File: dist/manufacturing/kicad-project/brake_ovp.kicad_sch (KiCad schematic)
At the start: 13 parts, among them J3 B2P-VH(LF)(SN), Q16 CSD19534Q5A, U14 TLV3201AIDBVR, U15 UCC27511DBVR

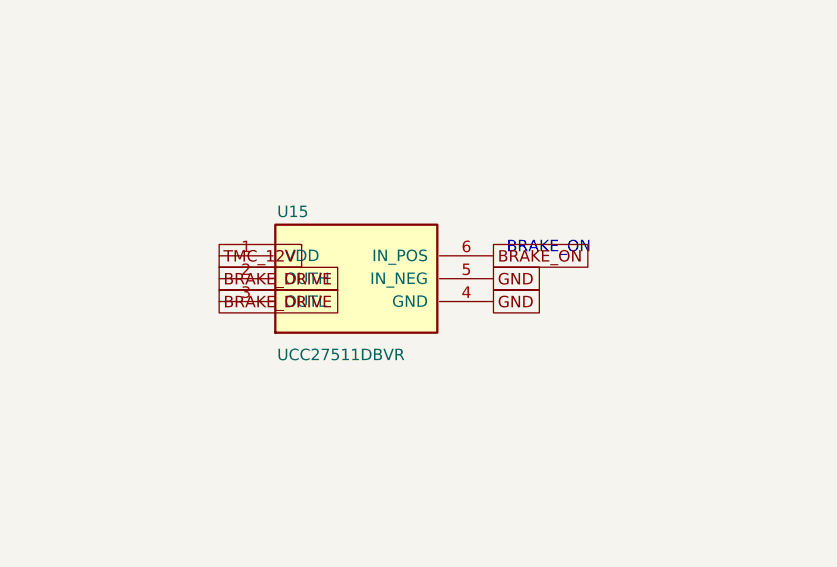
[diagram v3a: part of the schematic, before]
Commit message: Replace unavailable MCU and expander with stocked JLC parts
Use STM32G0B1CEU6 with a grounded UFQFPN48 exposed pad and a 512 KiB
firmware/readback target. Use PCA9538PWR with a PD-powered reset buffer,
bypass capacitor and pulldown to address independent-rail reset injection.

Regenerate local routing, native/manufacturing artifacts, assembly data,
stock evidence and the routed viewer. Preserve unrelated copper and holes
with the existing protected projection. Retain motion locks and physical
qualification holds. Preserve quoted DSN net names and native EP paste sizing.
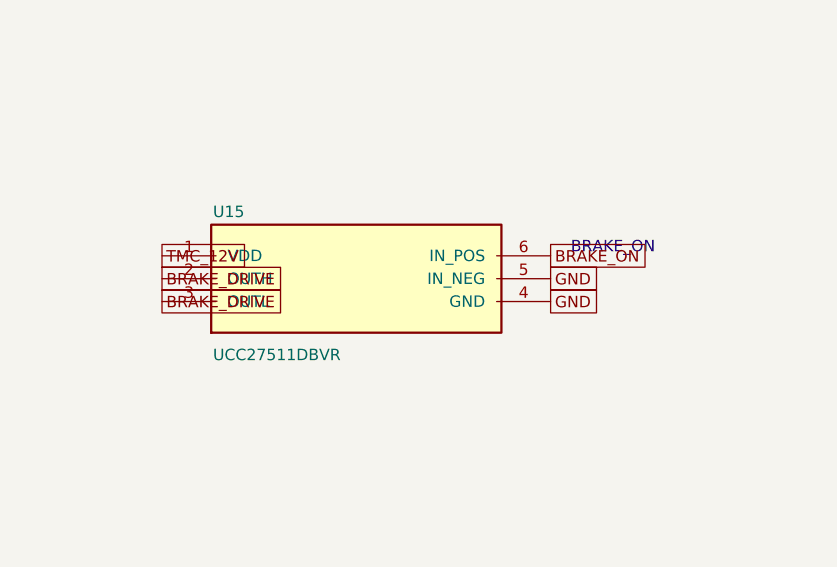
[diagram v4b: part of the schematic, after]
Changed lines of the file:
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@@
     (instances
       (project ""
-        (path "/857a17cf-af0e-42f8-87e7-32303329b4d2/9c455ead-0a67-4132-9c5a-187d55c8c2bc"
+        (path "/bf863bdb-065f-43fb-bcd3-832b382d0aae/5b88888b-e70e-43af-ad8f-c494d106280e"
           (reference "U14")
           (unit 1)
@@
     (instances
       (project ""
-        (path "/857a17cf-af0e-42f8-87e7-32303329b4d2/9c455ead-0a67-4132-9c5a-187d55c8c2bc"
+        (path "/bf863bdb-065f-43fb-bcd3-832b382d0aae/5b88888b-e70e-43af-ad8f-c494d106280e"
           (reference "R64")
           (unit 1)
@@
     (instances
       (project ""
-        (path "/857a17cf-af0e-42f8-87e7-32303329b4d2/9c455ead-0a67-4132-9c5a-187d55c8c2bc"
+        (path "/bf863bdb-065f-43fb-bcd3-832b382d0aae/5b88888b-e70e-43af-ad8f-c494d106280e"
           (reference "R65")
           (unit 1)
@@
     (instances
       (project ""
-        (path "/857a17cf-af0e-42f8-87e7-32303329b4d2/9c455ead-0a67-4132-9c5a-187d55c8c2bc"
+        (path "/bf863bdb-065f-43fb-bcd3-832b382d0aae/5b88888b-e70e-43af-ad8f-c494d106280e"
           (reference "R66")
           (unit 1)
@@
     (instances
       (project ""
-        (path "/857a17cf-af0e-42f8-87e7-32303329b4d2/9c455ead-0a67-4132-9c5a-187d55c8c2bc"
+        (path "/bf863bdb-065f-43fb-bcd3-832b382d0aae/5b88888b-e70e-43af-ad8f-c494d106280e"
           (reference "R67")
           (unit 1)
@@
     (instances
       (project ""
-        (path "/857a17cf-af0e-42f8-87e7-32303329b4d2/9c455ead-0a67-4132-9c5a-187d55c8c2bc"
+        (path "/bf863bdb-065f-43fb-bcd3-832b382d0aae/5b88888b-e70e-43af-ad8f-c494d106280e"
           (reference "C41")
           (unit 1)
@@
     (property "Reference" "U15"
       (id 0)
-      (at 383.6325 237.675 0)
+      (at 376.5075 237.675 0)
       (effects
         (font
@@
     (property "Value" "UCC27511DBVR"
       (id 1)
-      (at 383.6325 253.575 0)
+      (at 376.5075 253.575 0)
       (effects
         (font
@@
     (instances
       (project ""
-        (path "/857a17cf-af0e-42f8-87e7-32303329b4d2/9c455ead-0a67-4132-9c5a-187d55c8c2bc"
+        (path "/bf863bdb-065f-43fb-bcd3-832b382d0aae/5b88888b-e70e-43af-ad8f-c494d106280e"
           (reference "U15")
           (unit 1)
@@
     (instances
       (project ""
-        (path "/857a17cf-af0e-42f8-87e7-32303329b4d2/9c455ead-0a67-4132-9c5a-187d55c8c2bc"
+        (path "/bf863bdb-065f-43fb-bcd3-832b382d0aae/5b88888b-e70e-43af-ad8f-c494d106280e"
           (reference "C42")
           (unit 1)
@@
     (instances
       (project ""
-        (path "/857a17cf-af0e-42f8-87e7-32303329b4d2/9c455ead-0a67-4132-9c5a-187d55c8c2bc"
+        (path "/bf863bdb-065f-43fb-bcd3-832b382d0aae/5b88888b-e70e-43af-ad8f-c494d106280e"
           (reference "C43")
           (unit 1)
@@
     (instances
       (project ""
-        (path "/857a17cf-af0e-42f8-87e7-32303329b4d2/9c455ead-0a67-4132-9c5a-187d55c8c2bc"
+        (path "/bf863bdb-065f-43fb-bcd3-832b382d0aae/5b88888b-e70e-43af-ad8f-c494d106280e"
           (reference "R68")
           (unit 1)
@@
     (instances
       (project ""
-        (path "/857a17cf-af0e-42f8-87e7-32303329b4d2/9c455ead-0a67-4132-9c5a-187d55c8c2bc"
+        (path "/bf863bdb-065f-43fb-bcd3-832b382d0aae/5b88888b-e70e-43af-ad8f-c494d106280e"
           (reference "R69")
           (unit 1)
@@
     (instances
       (project ""
-        (path "/857a17cf-af0e-42f8-87e7-32303329b4d2/9c455ead-0a67-4132-9c5a-187d55c8c2bc"
+        (path "/bf863bdb-065f-43fb-bcd3-832b382d0aae/5b88888b-e70e-43af-ad8f-c494d106280e"
           (reference "Q16")
           (unit 1)
@@
     (instances
       (project ""
-        (path "/857a17cf-af0e-42f8-87e7-32303329b4d2/9c455ead-0a67-4132-9c5a-187d55c8c2bc"
+        (path "/bf863bdb-065f-43fb-bcd3-832b382d0aae/5b88888b-e70e-43af-ad8f-c494d106280e"
           (reference "J3")
           (unit 1)
@@
   )
   (text "BRAKE_ON"
-    (at 409.1325 241.725 0)
+    (at 416.2575 241.725 0)
     (effects
       (font
@@
   (global_label "TMC_12V"
     (shape passive)
-    (at 377.19 242.57000000000002 0)
+    (at 370.84000000000003 242.57000000000002 0)
     (effects
       (font
@@
   (global_label "BRAKE_DRIVE"
     (shape passive)
-    (at 377.19 245.11 0)
+    (at 370.84000000000003 245.11 0)
     (effects
       (font
@@
   (global_label "BRAKE_DRIVE"
     (shape passive)
-    (at 377.19 247.65 0)
+    (at 370.84000000000003 247.65 0)
     (effects
       (font
@@
   (global_label "GND"
     (shape passive)
-    (at 407.67 247.65 0)
+    (at 414.02 247.65 0)
     (effects
       (font
@@
   (global_label "GND"
     (shape passive)
-    (at 407.67 245.11 0)
+    (at 414.02 245.11 0)
     (effects
       (font
@@
   (global_label "BRAKE_ON"
     (shape passive)
-    (at 407.67 242.57000000000002 0)
-    (effects
-      (font
+    (at 414.02 242.57000000000002 0)
+    (effects
+      (font
